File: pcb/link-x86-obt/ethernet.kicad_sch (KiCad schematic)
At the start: 39 parts, among them J6 74990101241, U2 W5500, Y1 25MHz

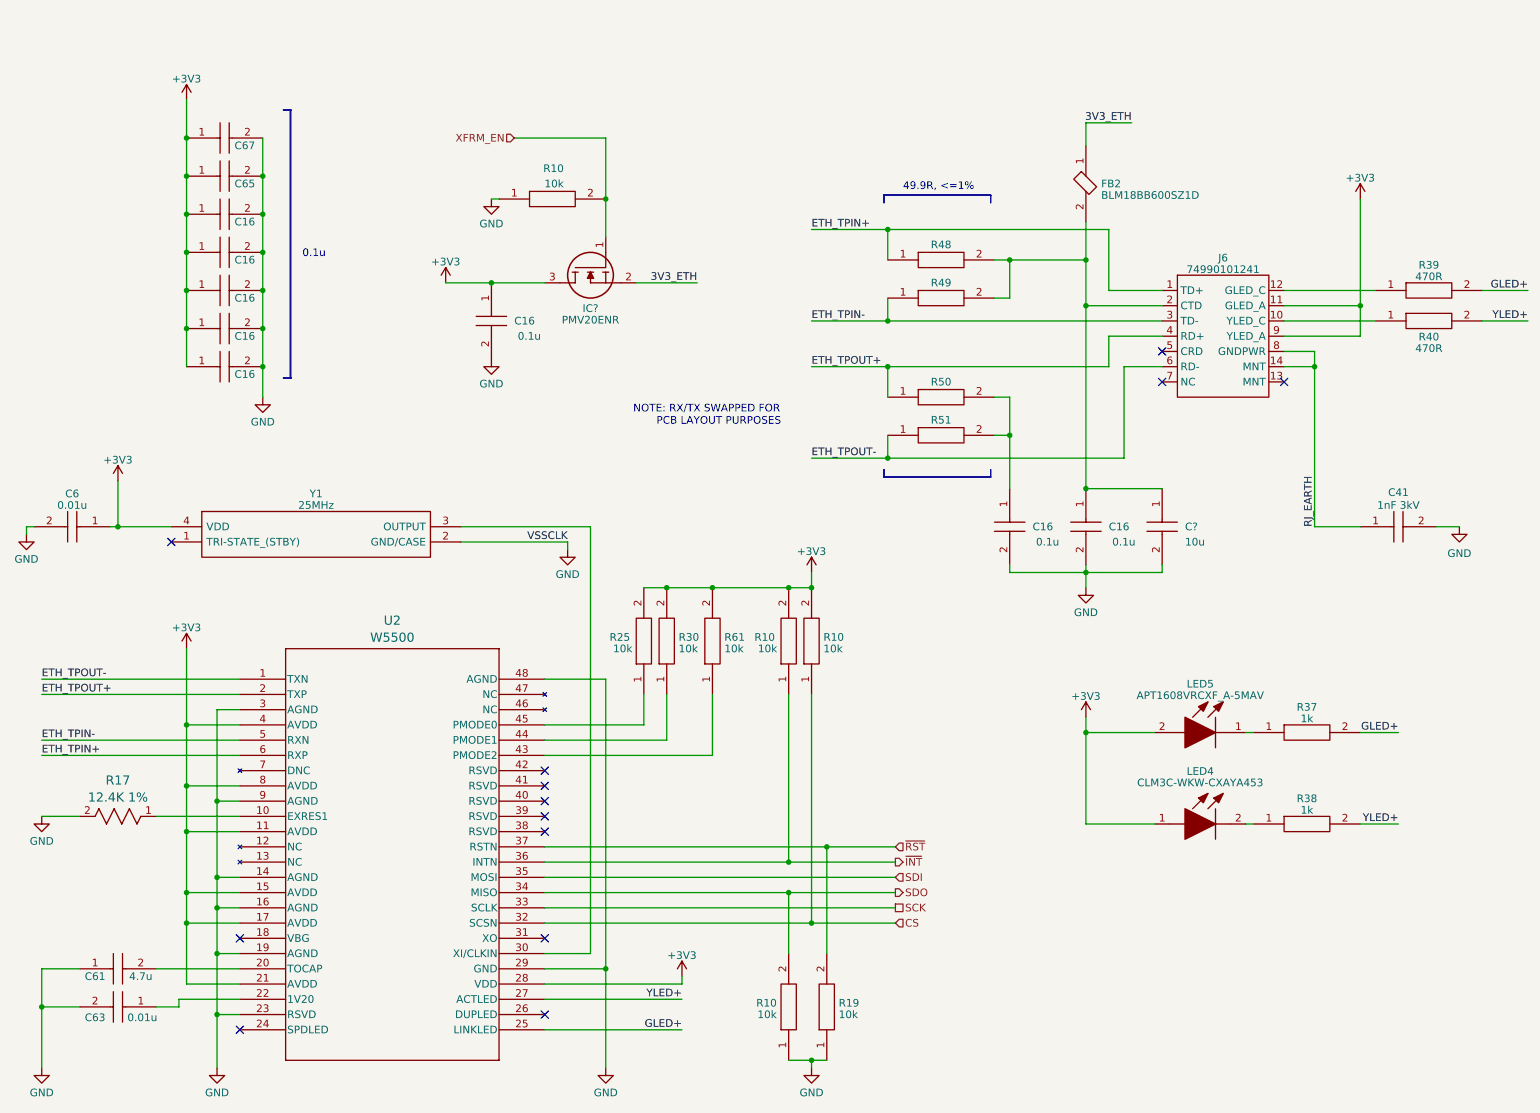
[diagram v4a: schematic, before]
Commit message: next iteration of ethernet port schematic
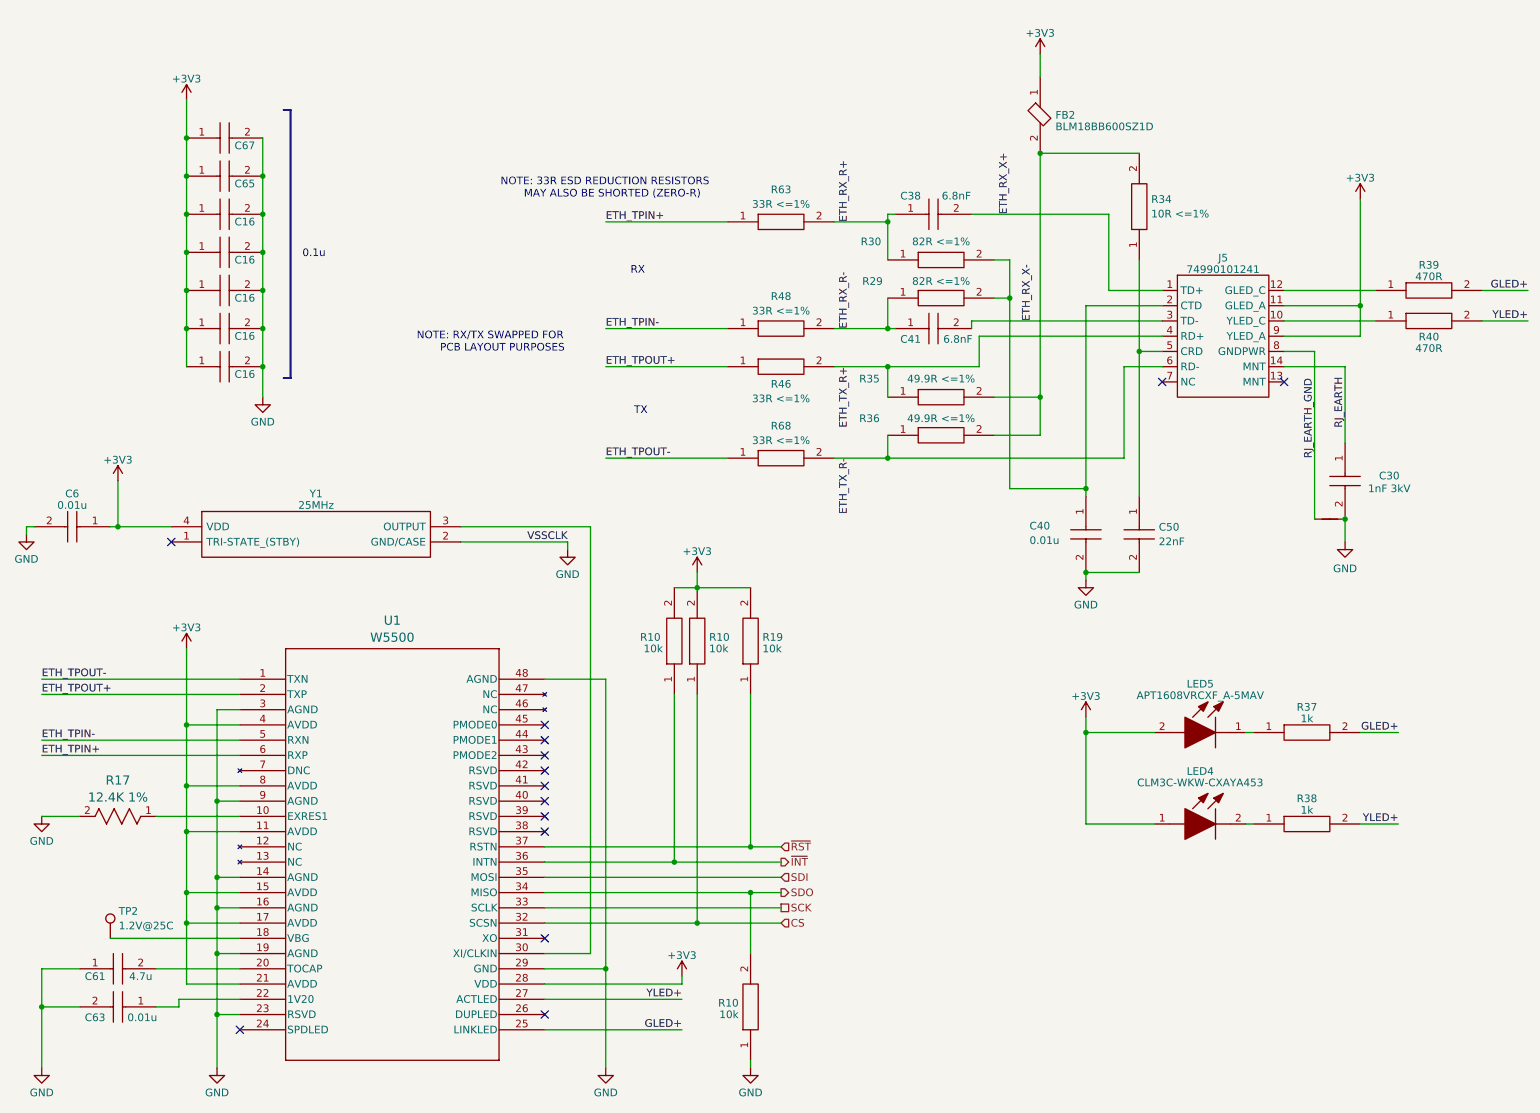
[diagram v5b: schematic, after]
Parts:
- removed C16 (x3): 0.1u, CAPC1005X33N, symbol Oro:MSAST1L3YB5104KFNA01
- removed C41: 1nF 3kV, CAPC4620X220N, symbol SamacSys_Parts:885342210004
- removed C?: 10u, SamacSys_Parts:CAPC2012X135N, symbol SamacSys_Parts:LMK212ABJ106KG8T
- removed IC?: PMV20ENR, SamacSys_Parts:SOT95P230X110-3N, symbol SamacSys_Parts:CSD13380F3T
- removed R10, R25, R30, R61: 10k, RESC1005X40N, symbol SamacSys_Parts:RK73H1ETTP1002F
- removed R48, R49: RMCF0201FT49R9, RESC1005X35N, symbol SamacSys_Parts:RT0402FRE0749R9L
- added C30: 1nF 3kV, CAPC4620X220N, symbol SamacSys_Parts:885342210004
- added C38, C41: 6.8nF, CAPC1608X87N, symbol SamacSys_Parts:C0603C682F5GACTU
- added C40: 0.01u, SamacSys_Parts:CAPC2012X75N, symbol SamacSys_Parts:CL21B103KBANNNC
- added C50: 22nF, CAPC1005X55N, symbol SamacSys_Parts:CC0402ZPY5V7BB223
- added NT1: NetTie_2, NetTie:NetTie-2_SMD_Pad0.5mm, symbol Device:NetTie_2
- added R29, R30: 82R <=1%, ERA2AED122X, symbol SamacSys_Parts:ERA-2AEB820X
- added R34: 10R <=1%, RESC0603X26N, symbol SamacSys_Parts:AC0201FR-0710RL
- added R46, R48, R63, R68: 33R <=1%, RCS0402_E3, symbol SamacSys_Parts:RCS040233R0FKED
- added TP2: 1.2V@25C, symbol Connector:TestPoint
- R35: renamed from R50; value RMCF0201FT49R9 -> 49.9R <=1%
- R36: renamed from R51; value RMCF0201FT49R9 -> 49.9R <=1%
- renumbered J6 to J5, U2 to U1
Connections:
- net 3V3_ETH is gone; now on net +3V3: FB2.1
- net +3V3: now also R19.2
- net ETH_TPIN+: now also R63.1; no longer J5.1 (TD+)
- net ETH_TPIN-: now also R48.1; no longer J5.3 (TD-)
- net ETH_TPOUT+: now also R46.1; no longer J5.4 (RD+), R35.1
- net ETH_TPOUT-: now also R68.1; no longer J5.6 (RD-), R36.1
- net GND: now also C30.2, C40.2, C50.2, NT1.2; no longer R19.1
- net RJ_EARTH: now also C30.1; no longer J5.8 (GNDPWR)
- net ~{RST}: now also R19.1; no longer R19.2
- net at J5.2 (CTD): now also C40.1, R29.2, R30.2; no longer FB2.2
- net at U1.18 (VBG): now also TP2.1
- net at R35.2, R36.2: now also FB2.2, R34.2
- net at J5.5 (CRD): now also C50.1, R34.1
- new net ETH_RX_R+: C38.1, R30.1, R63.2
- new net ETH_RX_R-: C41.1, R29.1, R48.2
- new net ETH_RX_X+: C38.2, J5.1 (TD+)
- new net ETH_RX_X-: C41.2, J5.3 (TD-)
- new net ETH_TX_R+: J5.4 (RD+), R35.1, R46.2
- new net ETH_TX_R-: J5.6 (RD-), R36.1, R68.2
- new net RJ_EARTH_GND: J5.8 (GNDPWR), NT1.1
- no-connect marks 13 -> 14
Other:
- note added: "NOTE: 33R ESD REDUCTION RESISTORS MAY ALSO BE SHORTED (ZERO-R)"
- note added: "RX"
- note added: "TX"
- note removed: "49.9R, <=1%"
- moved on the sheet: FB2, R10, R19

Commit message: initial test of new board
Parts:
- added TP10, TP12, TP14, TP16, TP6, TP8: ~, Oro Footprints:TestPoint_0.25mm, symbol Connector:TestPoint
- TP2: footprint (none) -> TestPoint:TestPoint_Pad_D1.0mm
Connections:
- net CS: now also TP16.1
- net SCK: now also TP6.1
- net SDI: now also TP10.1
- net SDO: now also TP8.1
- net ~{INT}: now also TP12.1
- net ~{RST}: now also TP14.1
